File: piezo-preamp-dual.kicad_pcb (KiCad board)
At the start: 2 copper layers, 28 x 15 mm, 29 parts, among them J3 piezo, J4 piezo, J5 output, U1 OPA1677, U2 OPA1677, U3 OPA1677

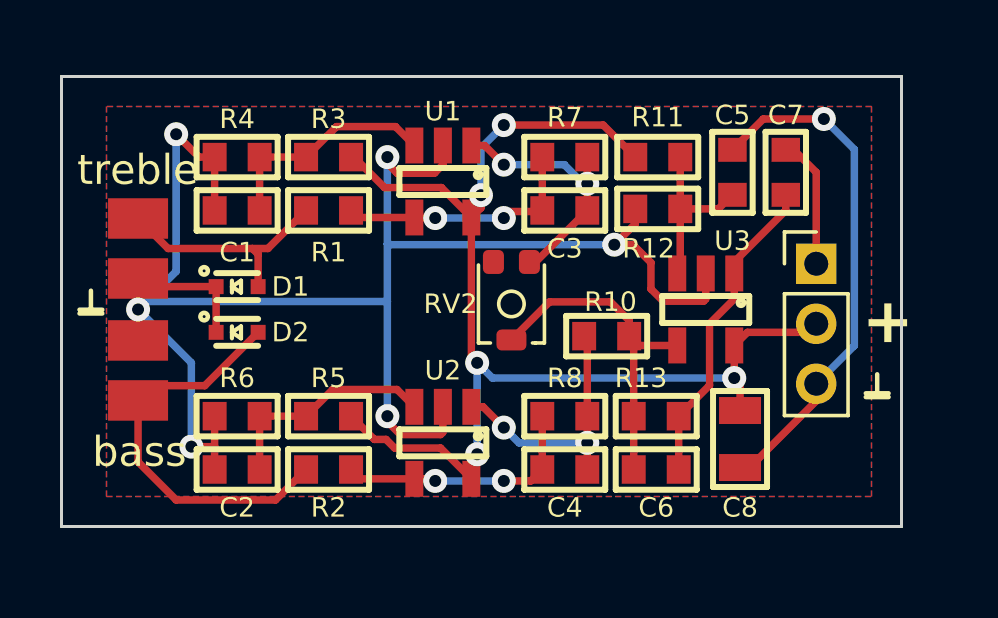
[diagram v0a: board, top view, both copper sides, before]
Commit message: The TVS diodes were removed from the "dual-channel" design. The PCB is slighly smaller as a result.
The parasitic capacitance of the TVS diodes had a negative effect on the sound. In addition, they were redundant; the inputs of the OPA1677 are already protected against overvoltage, so the 1 MOhm resistor is ample protection.

Signed-off-by: Thiadmer Riemersma <thiadmer@compuphase.com>
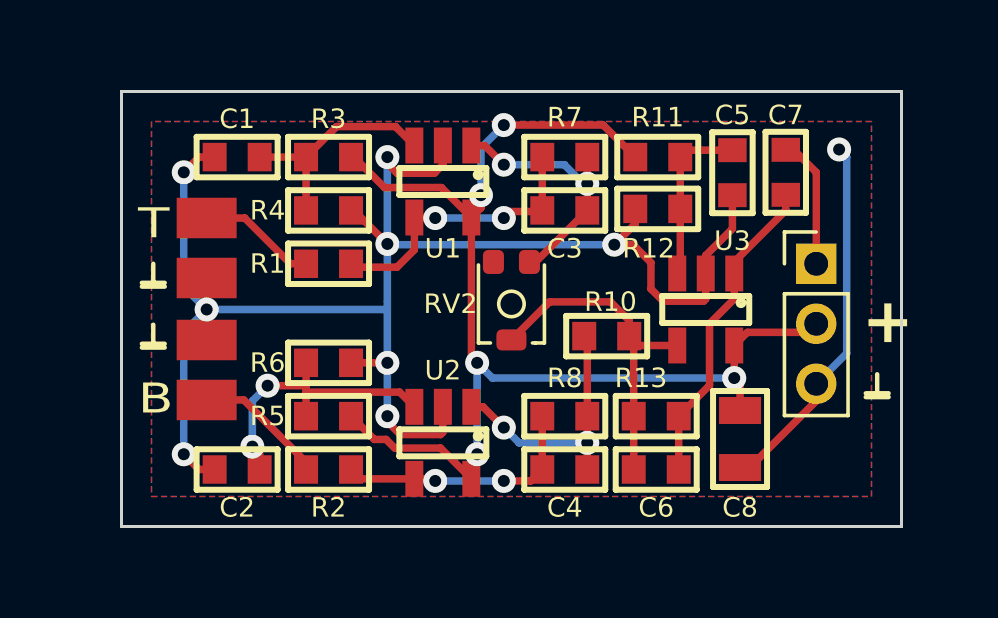
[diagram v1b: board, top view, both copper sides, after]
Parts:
- removed D1, D2: TVS 2V5, VisualPlace:SOD523
- C4, C6: value 39p -> 100p
- moved R6 3.53 mm to (104.9, 98.0), turned to 0 degrees
- moved R4 3.53 mm to (104.9, 93.0), turned to 0 degrees
- moved J3 2.29 mm to (100.8, 93.2)
- moved J4 2.29 mm to (100.8, 99.3)
- moved R1 1.78 mm to (104.9, 94.7)
- moved C1 1.78 mm to (101.9, 91.2)
- turned C5 to -90 degrees
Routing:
- net GND: track 78.6 -> 67.8 mm, vias 7 -> 9
- net Net-(J4-Pin_1): track 13.5 -> 4.42 mm
- net Net-(J3-Pin_1): track 7.89 -> 3.95 mm
- net Net-(U2-+): track 7.54 -> 9.99 mm, vias 0 -> 2
- net Net-(U1--): track 8.38 -> 9.65 mm
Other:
- board size 28 x 15 mm -> 26 x 14.5 mm
- board text added: "B"
- board text added: "T"
- board text removed: "bass"
- board text removed: "treble"

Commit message: Added bass-boost filter (dual-channel preamp only). Added Bill-Of-Materials file. Fixed PDF of the schematic (turned out to be unreadable).
Signed-off-by: Thiadmer Riemersma <thiadmer@compuphase.com>
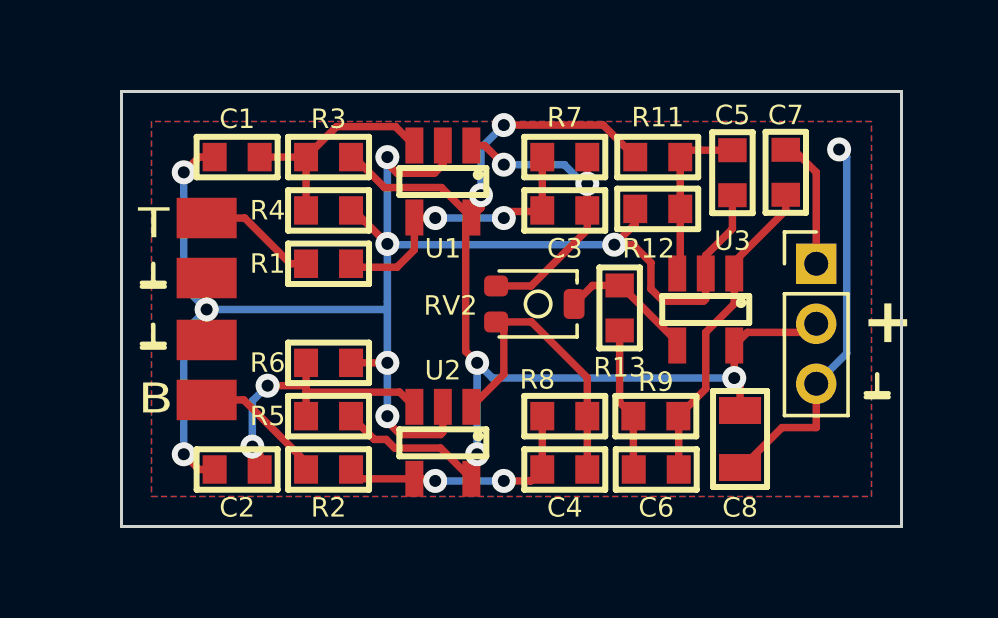
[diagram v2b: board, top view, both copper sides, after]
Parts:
- removed R10: 10k, VisualPlace:0603
- added R9: 47k, VisualPlace:0603, F.Cu at (115.8, 99.8)
- C3: value 39p -> 68p
- C4: value 100p -> 68p
- C6: value 100p -> 10n
- R11, R12, R13, R3, R4, R5, R6: value 47k -> 68k
- moved R13 3.81 mm to (114.6, 96.2), turned to -90 degrees
- moved RV2 0.89 mm to (111.9, 96.1), turned to 0 degrees
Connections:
- C6 pad 1: Net-(U3--) -> Net-(C6-Pad1)
- R13 pad 2: Net-(C6-Pad2) -> Net-(C6-Pad1)
- RV2 pad 3: unconnected-(RV2-Pad3) -> Net-(C4-Pad2)
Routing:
- net Net-(U3--): track 11.5 -> 4.59 mm
- net Net-(C6-Pad1): track 0.00 -> 4.83 mm
- net Net-(C3-Pad2): track 8.90 -> 10.7 mm
- net Net-(C4-Pad2): track 8.85 -> 10.3 mm, vias 2 -> 0
- net GND: track 67.8 -> 68.3 mm

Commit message: Reduce (peak) voltage of the piezo pick-ups, to avoid saturatating the opamps. Switch opamps to OPA323, to avoid clamping diodes on input. Higher input impedance.
Signed-off-by: thiadmer <thiadmer.riemersma@gmail.com>
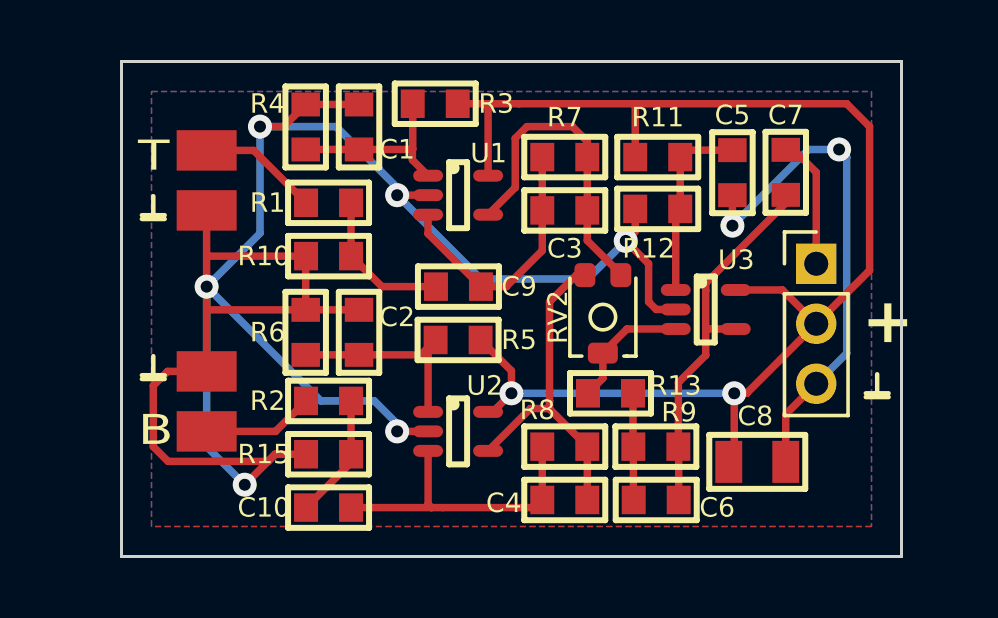
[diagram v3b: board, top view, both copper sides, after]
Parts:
- added C10: 100k, VisualPlace:0603, F.Cu at (104.9, 102.9)
- added C9: 100k, VisualPlace:0603, F.Cu at (109.2, 95.5)
- added R10: 100k, VisualPlace:0603, F.Cu at (104.9, 94.5)
- added R15: 100k, VisualPlace:0603, F.Cu at (104.9, 101.1)
- C6: value 10n -> 22n
- R1, R2: value 1M -> 2M2
- R11, R12, R3, R4, R5, R6: value 68k -> 100k
- R13: value 68k -> 22k
- R7, R8: value 1M -> 470k
- R9: value 47k -> 22k
- U1, U2, U3: value OPA1677 -> OPA323; footprint VisualPlace:SOT23-5 -> VisualPlace:SOT353
- moved C2 6.12 mm to (105.9, 97.0), turned to 90 degrees
- moved R5 5.01 mm to (109.2, 97.3)
- moved C1 4.19 mm to (105.9, 90.2), turned to 90 degrees
- moved R3 3.98 mm to (108.5, 89.4)
- moved R4 2.88 mm to (104.1, 90.2), turned to 90 degrees
- moved R13 2.86 mm to (114.3, 99.1), turned to 0 degrees
- moved R2 2.29 mm to (104.9, 99.3)
- moved J3 2.25 mm to (100.8, 91.0)
- moved RV2 2.20 mm to (114.0, 96.5), turned to -90 degrees
- moved R1 2.03 mm to (104.9, 92.7)
- moved R6 1.27 mm to (104.1, 97.0), turned to 90 degrees
- moved J4 1.05 mm to (100.8, 100.3)
- moved C4 1.02 mm to (112.8, 102.6)
- moved C6 1.02 mm to (115.8, 102.6)
- moved R8 1.02 mm to (112.8, 100.8)
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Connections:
- net +9V renamed +5V
- R1 pad 2: Net-(U1--) -> Net-(R1-Pad2)
- R2 pad 2: Net-(U2--) -> Net-(R15-Pad1)
- U1 pad 1: Net-(C3-Pad2) -> Net-(U1-+)
- U1 pad 3: Net-(U1-+) -> Net-(U1--)
- U1 pad 4: Net-(U1--) -> Net-(C3-Pad2)
- U2 pad 1: Net-(C4-Pad2) -> Net-(U2-+)
- U2 pad 3: Net-(U2-+) -> Net-(U2--)
- U2 pad 4: Net-(U2--) -> Net-(C4-Pad2)
- U3 pad 1: Net-(C6-Pad2) -> Net-(U3-+)
- U3 pad 3: Net-(U3-+) -> Net-(U3--)
- U3 pad 4: Net-(U3--) -> Net-(C6-Pad2)
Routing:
- net GND: track 68.3 -> 90.4 mm, vias 9 -> 8
- net Net-(R1-Pad2): track 0.00 -> 5.03 mm
- net +5V: track 41.1 -> 45.5 mm, vias 5 -> 2
- net Net-(R15-Pad1): track 0.00 -> 4.18 mm
- net Net-(U2-+): track 9.99 -> 7.04 mm, vias 2 -> 0
- net Net-(C6-Pad2): track 10.6 -> 12.7 mm
- net Net-(U2--): track 8.47 -> 10.2 mm, vias 2 -> 0
- net Net-(U1-+): track 7.62 -> 6.18 mm
- net Net-(C6-Pad1): track 4.83 -> 3.57 mm
- net Net-(C4-Pad2): track 10.3 -> 11.3 mm
- net Net-(U1--): track 9.65 -> 8.79 mm, vias 2 -> 0
- net Net-(J4-Pin_1): track 4.42 -> 3.73 mm
- net Net-(U3-+): track 5.76 -> 6.33 mm
- net Net-(C3-Pad2): track 10.7 -> 10.6 mm, vias 2 -> 0
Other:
- board size 26 x 14.5 mm -> 26 x 16.5 mm
